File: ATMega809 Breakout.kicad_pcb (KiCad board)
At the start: 2 copper layers, 77.9 x 41.4 mm, 47 parts, among them J1 USB_B_Micro, J2 Conn_01x05, J3 Conn_01x20, J4 Conn_01x12, J5 UPDI, Q1 PJA3438-AU, Q2 PJA3438-AU, Q3 PJA3438-AU, Q4 PJA3438-AU, Q5 PJA3438-AU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

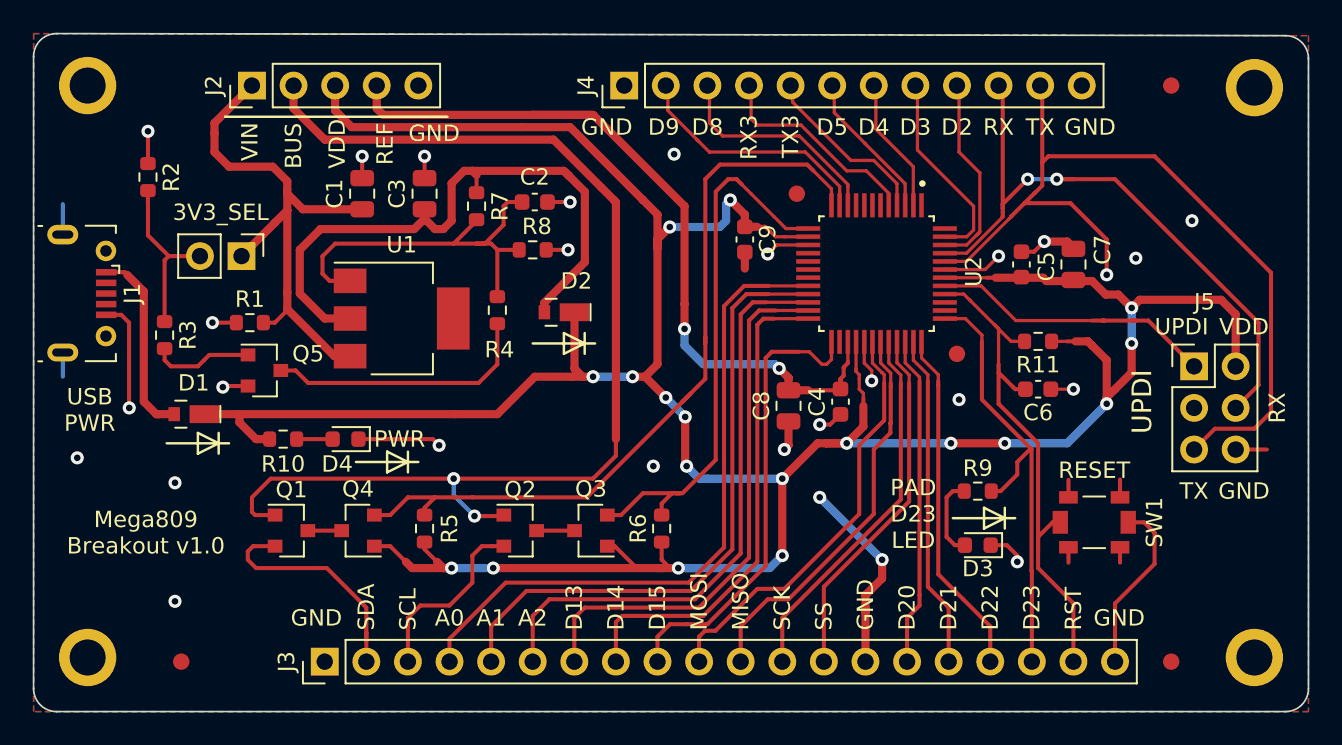
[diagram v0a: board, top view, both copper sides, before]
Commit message: Cleanup. Basically ready for mfg.
* Switched USB connectors to pure-SMT assembly, no THT.
* More trace clean-ups. Eliminated 45 deg angles in traces.
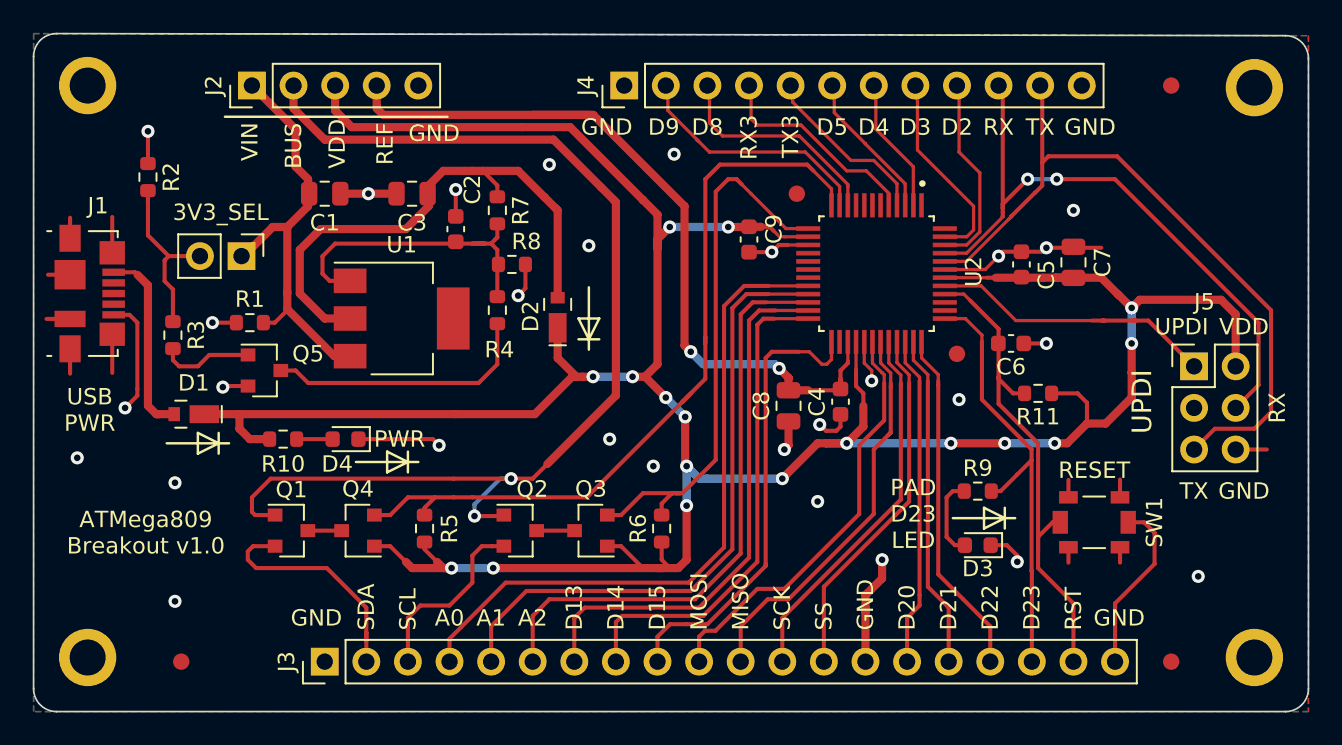
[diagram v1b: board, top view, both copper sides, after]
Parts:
- J1: footprint aaron-imported-parts:USB_Micro-B_AdamTech-MCR-B-S-RA-SMT-CS5A-NF -> aaron-imported-parts:USB_Micro-B_Molex_47346-1001
- moved C2 5.10 mm to (126.1, 44.3), turned to 270 degrees
- moved C6 3.25 mm to (160.0, 51.3)
- moved R11 3.18 mm to (161.7, 54.4)
- moved C1 2.29 mm to (118.1, 42.2), turned to 0 degrees
- moved R8 1.55 mm to (129.5, 46.5)
- moved R7 1.30 mm to (128.7, 43.2)
- moved C3 0.76 mm to (123.4, 42.2), turned to 180 degrees
- moved J1 0.51 mm to (103.8, 48.3)
- moved R3 0.51 mm to (108.8, 50.8)
- moved D2 0.49 mm to (132.3, 49.7), turned to 90 degrees
- moved C9 0.25 mm to (144.0, 45.0)
- moved C7 0.13 mm to (163.8, 46.4)
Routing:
- net /TX: track 54.4 -> 44.0 mm, vias 1 -> 0
- net VDD: track 198.2 -> 189.5 mm, vias 18 -> 17
- net VIN: track 34.9 -> 27.1 mm
- net GND: track 75.7 -> 83.1 mm, vias 27 -> 29
- net /VREG_OUT: track 39.0 -> 33.2 mm
- net /LINADJ: track 25.0 -> 19.7 mm
- net /RESET_L: track 33.4 -> 30.9 mm
- net VBUS: track 69.3 -> 67.9 mm
- net /D23: track 28.1 -> 27.4 mm
- net /RX: track 38.5 -> 38.0 mm
- net Net-(Q5-Pad1): track 6.24 -> 5.73 mm
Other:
- board text added: "ATMEGA809 BREAKOUT BOARD"
- board text added: "ATMega809 Breakout v1.0"
- board text added: "Max VIN: VDD + 3"
- board text added: "ROAR!"
- board text added: "SUPPLY POWER THROUGH VIN *OR* USB, NOT BOTH For 5V0 operation, VIN > 6.5V For 3V3 operation close jumper and VIN > 5.0V"
- board text removed: "GREMBLDUINO MEGA809 BREAKOUT BOARD"
- board text removed: "Mega809 Breakout v1.0"
- board text removed: "SUPPLY POWER THROUGH VIN *OR* USB, NOT BOTH For 5V0 operation, VIN > 6.5V For 3V3 operation close jumper and VIN > 5.5V"

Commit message: Improved RESET circuitry.
* Switch SW1 now discharges capacitor C6 to GND thru R12 (1K0) rather
  than short-circuit.
* Added resistor R13 (1K0) between RESET_L and pull-up R11/capacitor
  C6/SW1. If an external MCU drives RESET_L low, the capacitor will
  discharge through R13 rather than short circuit, limiting max
  discharge current encountered by the GPIO to 5mA.
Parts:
- added R12: 1K0, Resistor_SMD:R_0603_1608Metric, F.Cu at (169.4, 63.1)
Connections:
- SW1 pad 2: GND -> Net-(R12-Pad1)
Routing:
- net GND: track 83.1 -> 80.5 mm
- net Net-(R12-Pad1): track 0.00 -> 2.37 mm
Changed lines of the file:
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@@
     (thickness 1.6)
     (drawings 89)
-    (tracks 665)
+    (tracks 664)
     (zones 0)
-    (modules 47)
-    (nets 63)
+    (modules 48)
+    (nets 64)
   )
   (page A4)
@@
   (net 61 "Net-(D3-Pad2)")
   (net 62 "Net-(J5-Pad3)")
+  (net 63 "Net-(R12-Pad1)")
   (net_class Default "This is the default net class."
     (clearance 0.15)
@@
     (add_net "Net-(Q5-Pad1)")
     (add_net "Net-(Q5-Pad3)")
+    (add_net "Net-(R12-Pad1)")
     (add_net "Net-(U2-Pad1)")
     (add_net "Net-(U2-Pad16)")
@@
     (add_net VDD)
     (add_net VIN)
+  )
+  (module Resistor_SMD:R_0603_1608Metric (layer F.Cu)
+    (at 169.418 63.055 270)
+    (descr "Resistor SMD 0603 (1608 Metric), square (rectangular) end terminal, IPC_7351 nominal, (Body size source: IPC-SM-782 page 72, https://www.pcb-3d.com/wordpress/wp-content/uploads/ipc-sm-782a_amendment_1_and_2.pdf), generated with kicad-footprint-generator")
+    (tags resistor)
+    (attr smd)
+    (fp_text reference R12 (at 0 -1.43 90) (layer F.SilkS)
+      (effects (font (size 1 1) (thickness 0.15)))
+    )
+    (fp_text value 1K0 (at 0 1.43 90) (layer F.Fab)
+      (effects (font (size 1 1) (thickness 0.15)))
+    )
+    (fp_text user %R (at 0 0 90) (layer F.Fab)
+      (effects (font (size 0.4 0.4) (thickness 0.06)))
+    )
+    (fp_line (start -0.8 0.4125) (end -0.8 -0.4125) (layer F.Fab) (width 0.1))
+    (fp_line (start -0.8 -0.4125) (end 0.8 -0.4125) (layer F.Fab) (width 0.1))
+    (fp_line (start 0.8 -0.4125) (end 0.8 0.4125) (layer F.Fab) (width 0.1))
+    (fp_line (start 0.8 0.4125) (end -0.8 0.4125) (layer F.Fab) (width 0.1))
+    (fp_line (start -0.237258 -0.5225) (end 0.237258 -0.5225) (layer F.SilkS) (width 0.12))
+    (fp_line (start -0.237258 0.5225) (end 0.237258 0.5225) (layer F.SilkS) (width 0.12))
+    (fp_line (start -1.48 0.73) (end -1.48 -0.73) (layer F.CrtYd) (width 0.05))
+    (fp_line (start -1.48 -0.73) (end 1.48 -0.73) (layer F.CrtYd) (width 0.05))
+    (fp_line (start 1.48 -0.73) (end 1.48 0.73) (layer F.CrtYd) (width 0.05))
+    (fp_line (start 1.48 0.73) (end -1.48 0.73) (layer F.CrtYd) (width 0.05))
+    (pad 2 smd roundrect (at 0.825 0 270) (size 0.8 0.95) (layers F.Cu F.Paste F.Mask) (roundrect_rratio 0.25)
+      (net 1 GND))
+    (pad 1 smd roundrect (at -0.825 0 270) (size 0.8 0.95) (layers F.Cu F.Paste F.Mask) (roundrect_rratio 0.25)
+      (net 63 "Net-(R12-Pad1)"))
+    (model ${KISYS3DMOD}/Resistor_SMD.3dshapes/R_0603_1608Metric.wrl
+      (at (xyz 0 0 0))
+      (scale (xyz 1 1 1))
+      (rotate (xyz 0 0 0))
+    )
   )
   (module aaron-imported-parts:USB_Micro-B_Molex_47346-1001 (layer F.Cu)
@@
     (tags "SPST SPST_NO tactile PTS820")
     (attr smd)
-    (fp_text reference SW1 (at 3.683 0 90) (layer F.SilkS)
+    (fp_text reference SW1 (at 0.127 3.048 180) (layer F.SilkS)
       (effects (font (size 1 1) (thickness 0.15)))
     )
@@
       (net 1 GND))
     (pad 2 smd rect (at 2.075 0) (size 0.9398 1.397) (layers F.Cu F.Paste F.Mask)
-      (net 1 GND))
+      (net 63 "Net-(R12-Pad1)"))
     (pad 1 smd rect (at -2.075 0) (size 0.9398 1.397) (layers F.Cu F.Paste F.Mask)
       (net 6 /RESET_L))
@@
   (segment (start 166.675001 63.755001) (end 166.675001 64.567001) (width 0.25) (layer F.Cu) (net 1))
   (segment (start 166.675001 64.567001) (end 166.675001 64.694001) (width 0.25) (layer F.Cu) (net 1))
-  (segment (start 166.37 70.739) (end 166.37 67.183) (width 0.25) (layer F.Cu) (net 1))
-  (segment (start 166.37 67.183) (end 168.783 64.77) (width 0.25) (layer F.Cu) (net 1))
-  (segment (start 168.783 62.865) (end 168.148 62.23) (width 0.25) (layer F.Cu) (net 1))
-  (segment (start 168.783 64.77) (end 168.783 62.865) (width 0.25) (layer F.Cu) (net 1))
-  (segment (start 167.175 62.23) (end 168.148 62.23) (width 0.25) (layer F.Cu) (net 1))
   (segment (start 155.975 46.794) (end 158.057 46.794) (width 0.2) (layer F.Cu) (net 1))
   (via (at 159.258 45.974) (size 0.8) (drill 0.4) (layers F.Cu B.Cu) (net 1))
@@
   (via (at 135.509 57.15) (size 0.8) (drill 0.4) (layers F.Cu B.Cu) (net 1))
   (segment (start 129.921 48.387) (end 130.365 47.943) (width 0.25) (layer F.Cu) (net 1))
+  (segment (start 169.418 63.88) (end 169.418 65.405) (width 0.25) (layer F.Cu) (net 1))
+  (segment (start 169.418 65.405) (end 166.37 68.453) (width 0.25) (layer F.Cu) (net 1))
+  (segment (start 166.37 68.453) (end 166.37 70.739) (width 0.25) (layer F.Cu) (net 1))
   (segment (start 118.696 52.084) (end 115.824 49.212) (width 0.5) (layer F.Cu) (net 2))
   (segment (start 119.659 52.084) (end 118.696 52.084) (width 0.5) (layer F.Cu) (net 2))
@@
   (segment (start 156.591 63.627) (end 156.083 63.119) (width 0.25) (layer F.Cu) (net 61))
   (segment (start 157.353 63.627) (end 156.591 63.627) (width 0.25) (layer F.Cu) (net 61))
+  (segment (start 167.175 62.23) (end 169.545 62.23) (width 0.25) (layer F.Cu) (net 63))
   (zone (net 1) (net_name GND) (layer F.Cu) (hatch edge 0.508)
     (connect_pads (clearance 0.508))

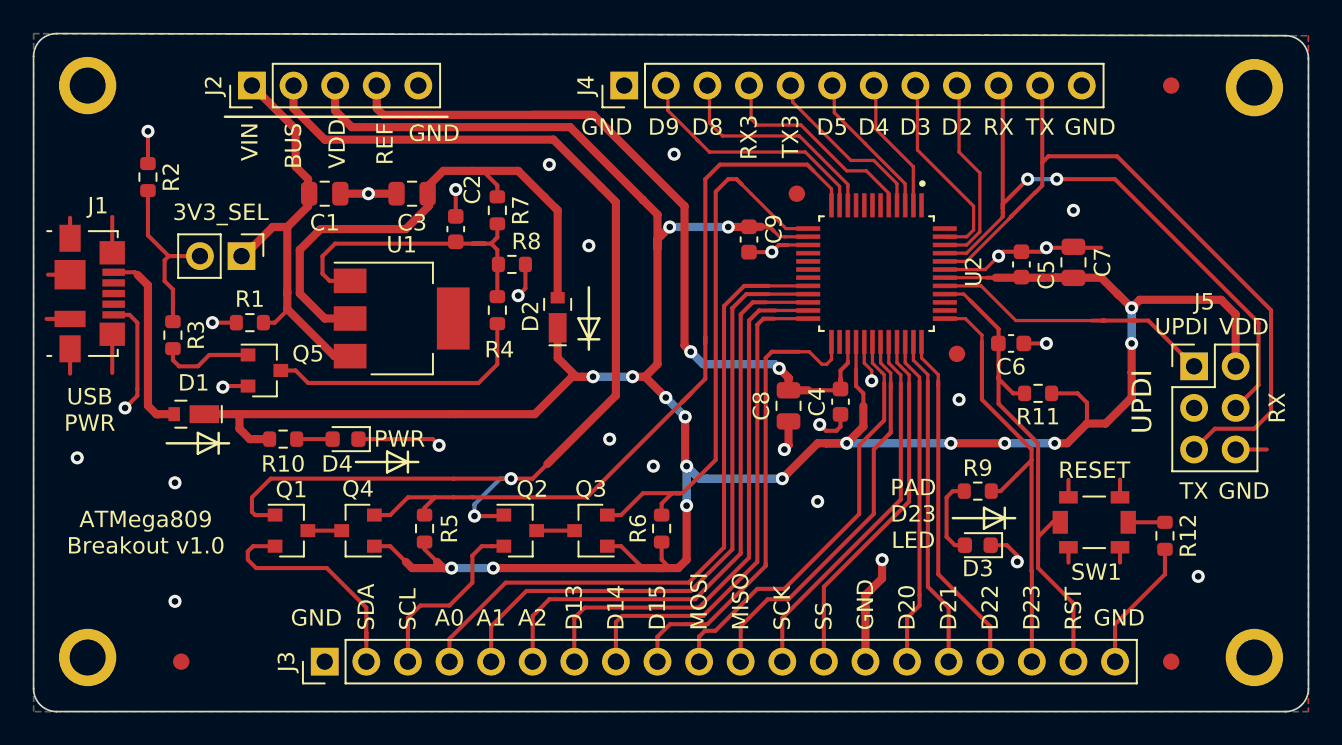
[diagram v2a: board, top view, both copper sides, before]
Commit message: Add resistor R14 between UPDI_MCU and UPDI pin.
If the MCU and programmer get out of sync and each try to drive the line
in different directions, somebody's going to have a bad time. Small
resistor ensures device safety while allowing high-speed bandwidth.
Value is sufficiently low that even if the programmer also has a 470R
on the line the logic levels will still work OK.

See discussion:
https://github.com/SpenceKonde/AVR-Guidance/blob/master/HardwareNotes/UPDISeriesResistors.md
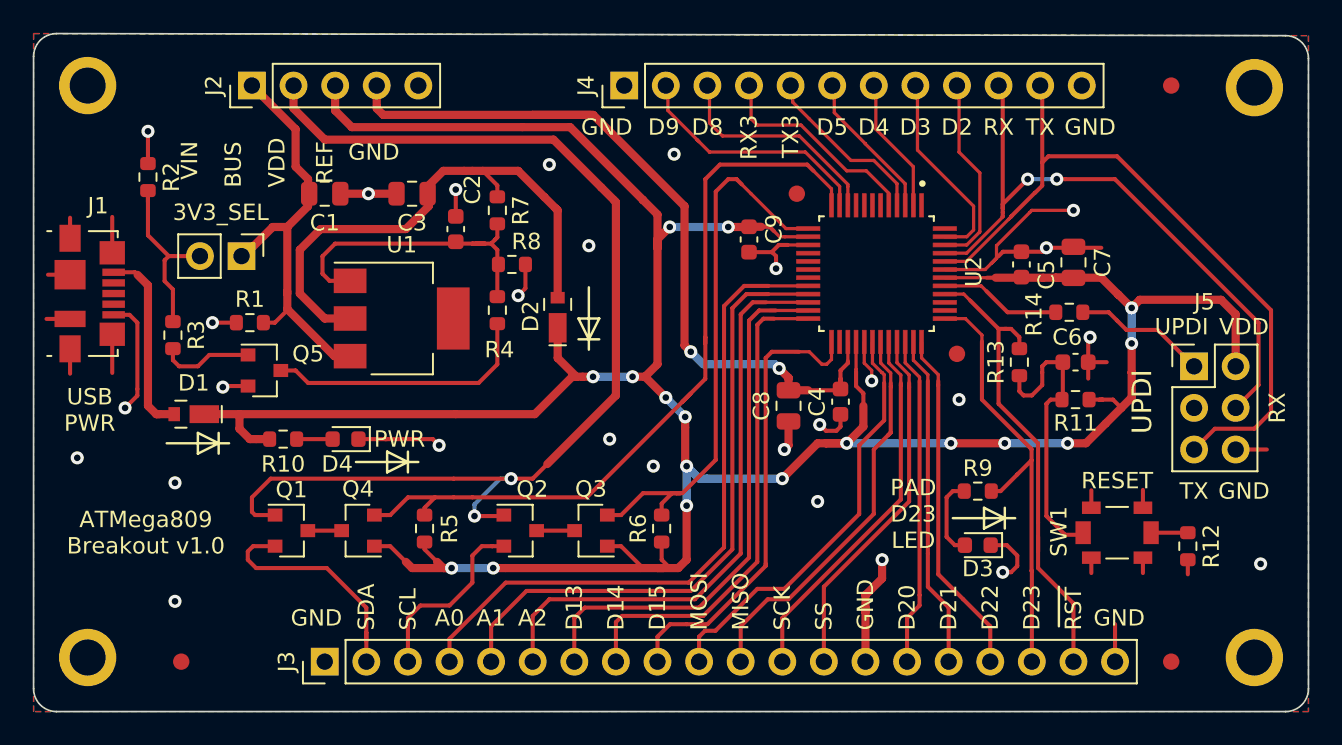
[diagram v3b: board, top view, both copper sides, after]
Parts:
- added R13: 1K0, Resistor_SMD:R_0603_1608Metric, F.Cu at (160.5, 52.5)
- added R14: 470R, Resistor_SMD:R_0603_1608Metric, F.Cu at (163.6, 49.4)
- moved C6 4.10 mm to (164.0, 52.5)
- moved R11 2.32 mm to (164.0, 54.7)
- moved SW1 1.53 mm to (166.5, 62.9)
- moved R12 1.53 mm to (170.8, 63.7)
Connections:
- C6 pad 2: /RESET_L -> Net-(C6-Pad2)
- J5 pad 1: /UPDI -> UPDI
- R11 pad 2: /RESET_L -> Net-(C6-Pad2)
- SW1 pad 1: /RESET_L -> Net-(C6-Pad2)
- U2 pad 41: /UPDI -> /UPDI_MCU
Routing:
- net Net-(C6-Pad2): track 0.00 -> 18.3 mm
- net /UPDI: track 17.8 -> 0.00 mm
- net UPDI: track 0.00 -> 8.34 mm
- net /UPDI_MCU: track 0.00 -> 7.44 mm
- net GND: track 80.5 -> 87.2 mm, vias 29 -> 28
- net /RESET_L: track 30.9 -> 29.0 mm
- net VDD: track 189.5 -> 188.2 mm

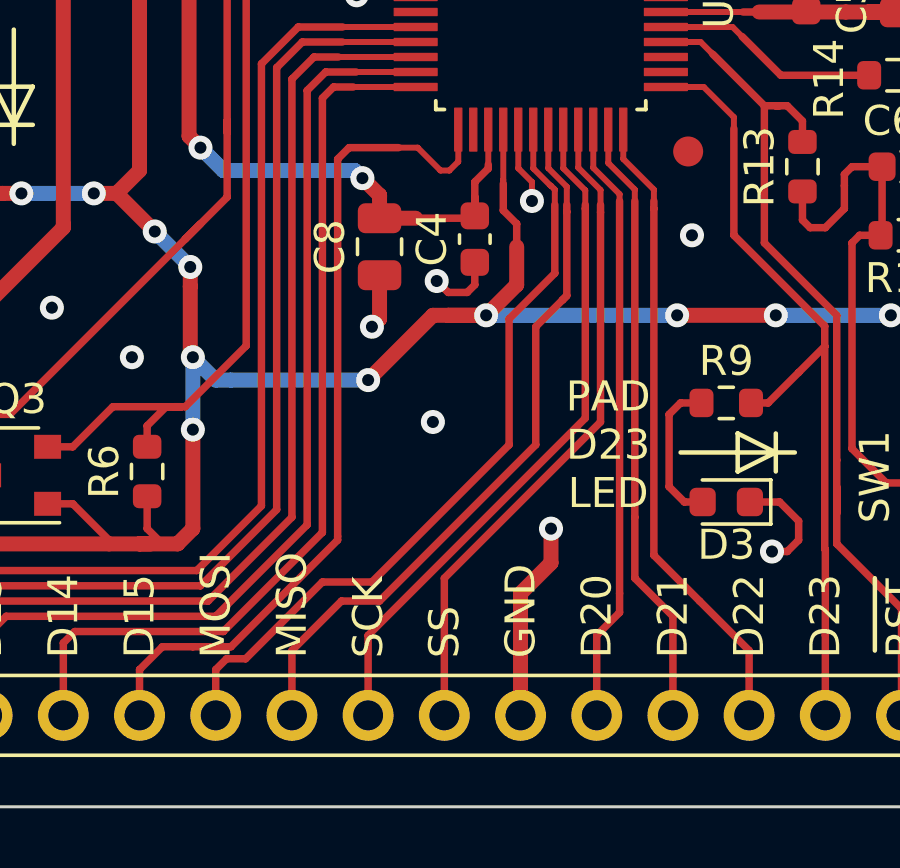
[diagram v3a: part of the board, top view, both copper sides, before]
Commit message: Add decoupling cap C10 for AVDD pin of MCU.
Add 100nF stabilizing ballast to AVDD input (MCU pin 28).
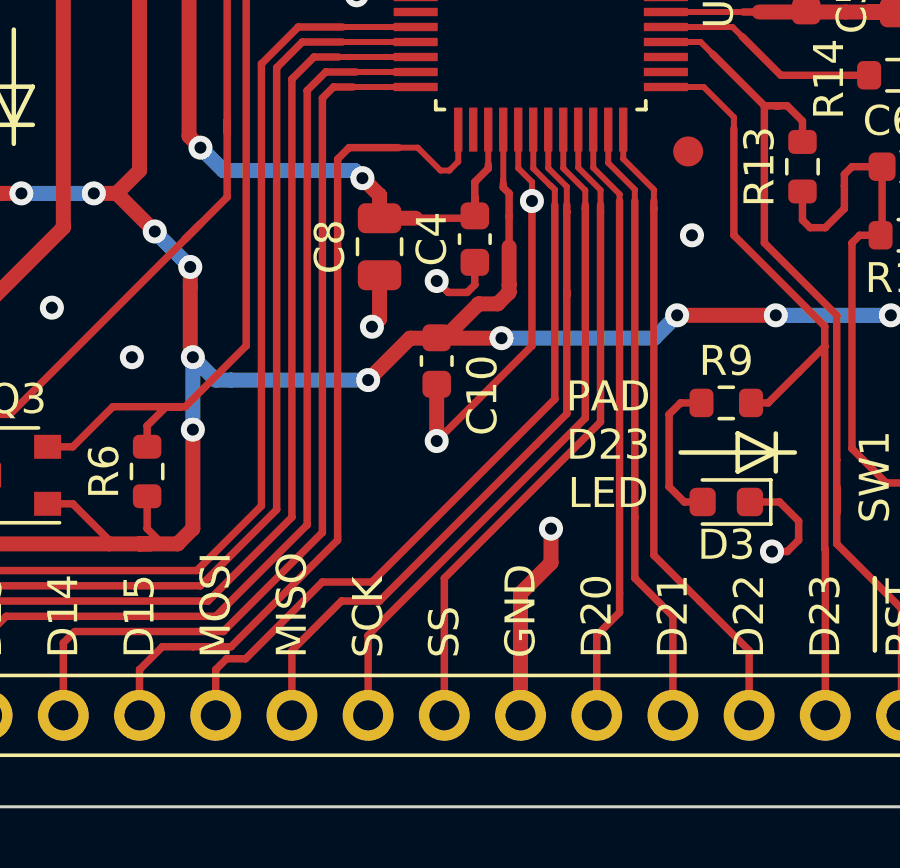
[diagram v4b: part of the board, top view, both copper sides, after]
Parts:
- added C10: 100n, Capacitor_SMD:C_0603_1608Metric, F.Cu at (148.3, 58.9)
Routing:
- net GND: track 87.2 -> 98.4 mm
